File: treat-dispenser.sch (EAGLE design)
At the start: 36 parts, among them U1 MCP73831, U3 ATMEGA32U4, Y1 16MHz

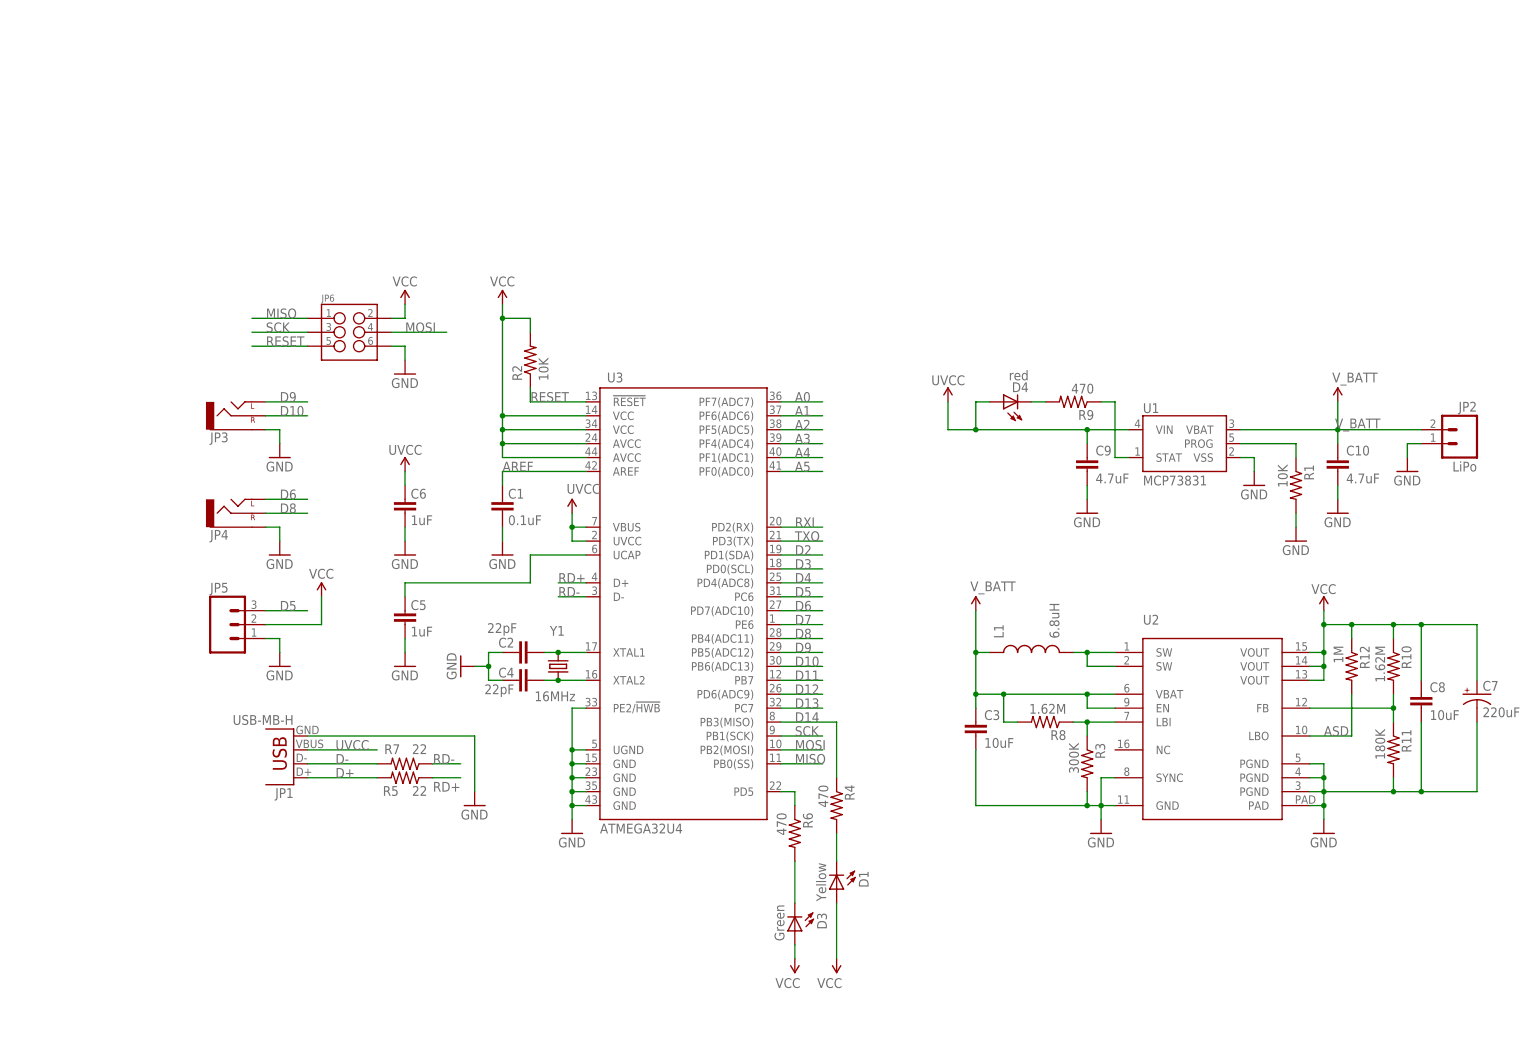
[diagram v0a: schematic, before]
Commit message: fixed some routing issues, added part numbers
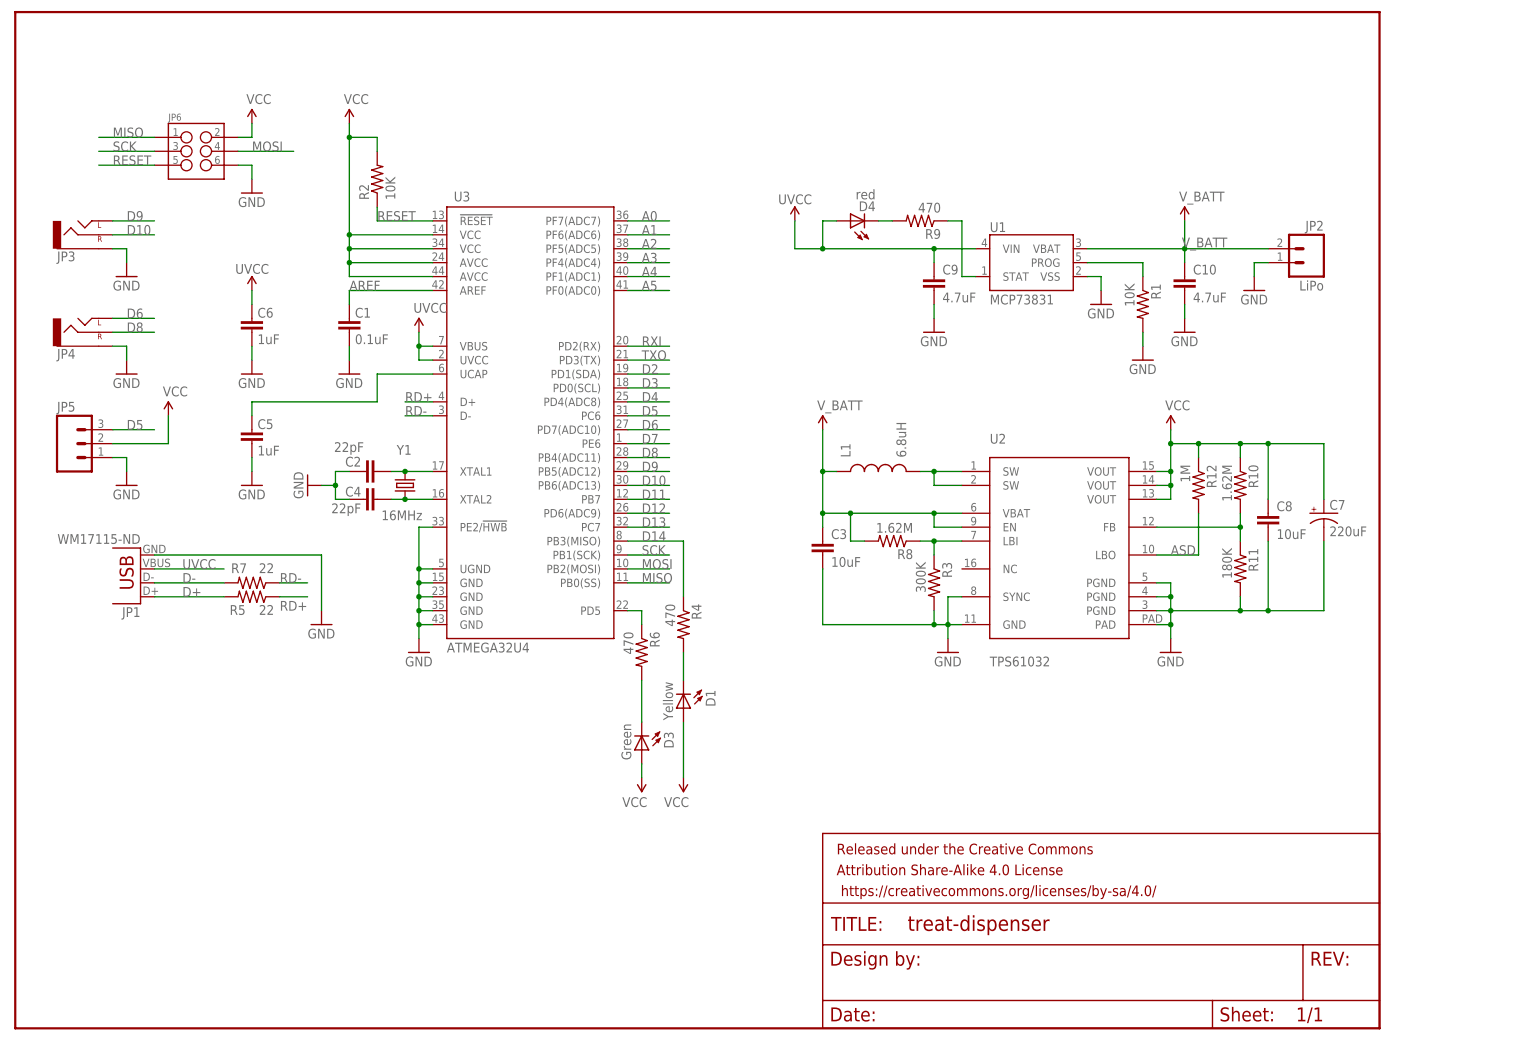
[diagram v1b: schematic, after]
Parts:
- added FRAME1: FRAME-LETTER, SparkFun-Aesthetics:FRAME-LETTER
- JP1: value USB-MB-H -> WM17115-ND
- U2: value (none) -> TPS61032
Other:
- moved on the sheet: C1, C10, C2, C3, C4, C5, C6, C7, C8, C9, D1, D3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

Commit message: minor fixes and part changes, added status led
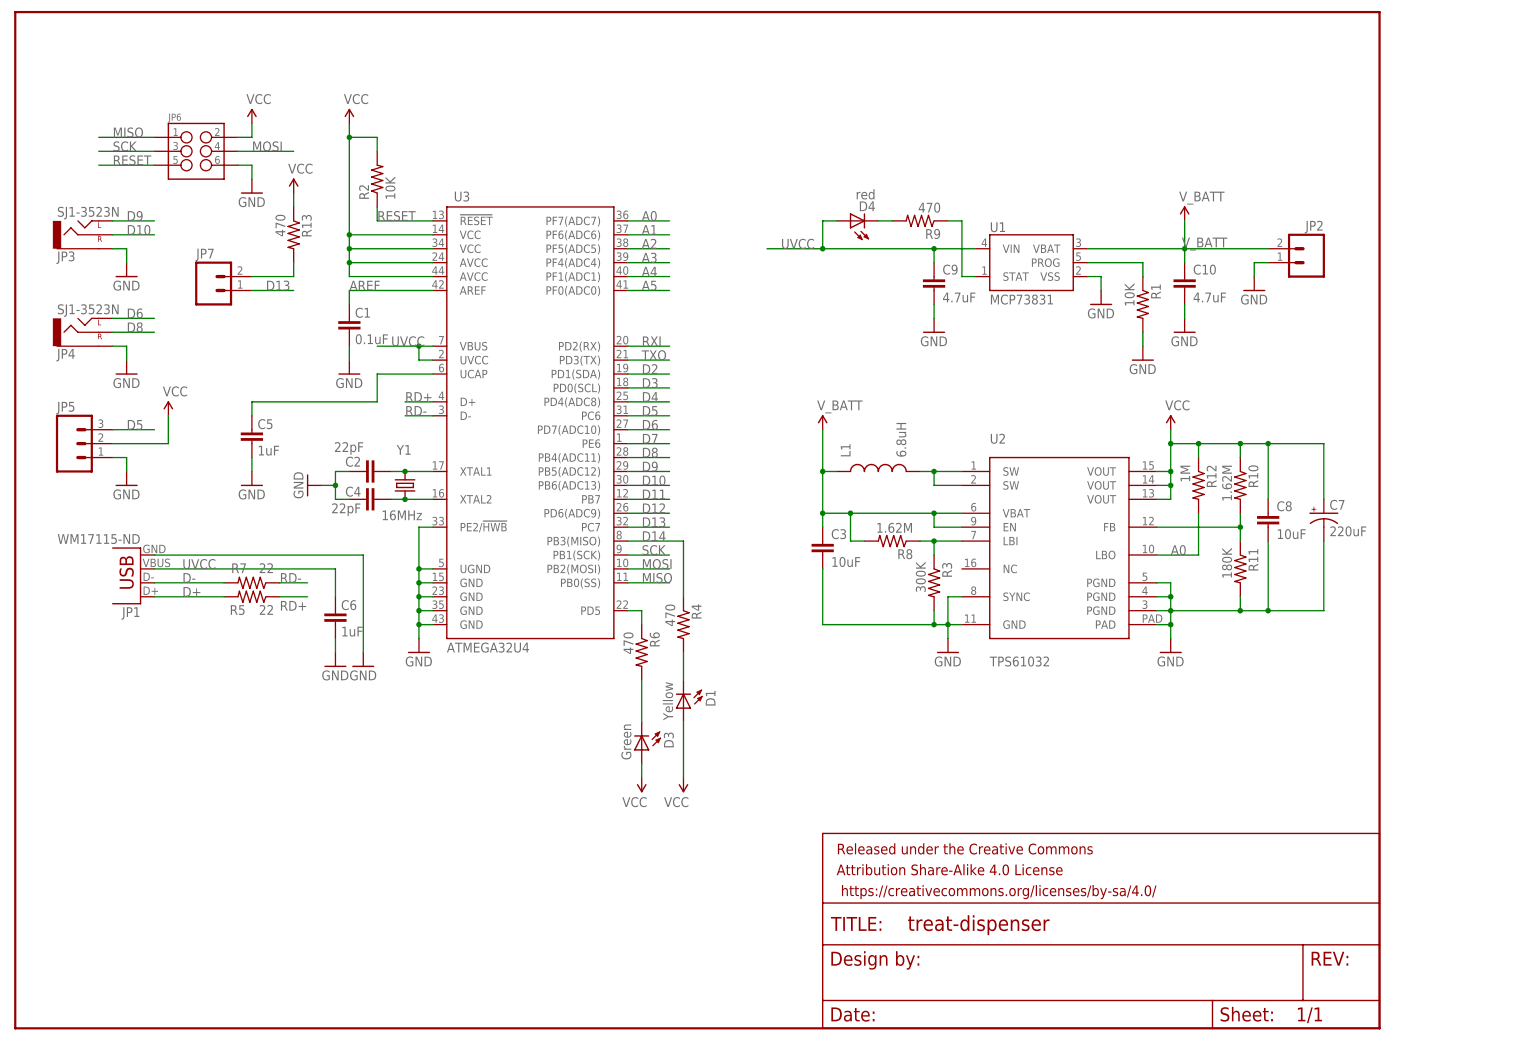
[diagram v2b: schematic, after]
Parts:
- added JP7: (no value), SparkFun-Connectors:M02PTH
- added R13: 470, SparkFun:RESISTOR0603-RES
- JP2: value LiPo -> (none); device SparkFun:M02-JST-2MM-SMT -> SparkFun-Connectors:M02JST-PTH-2-KIT
- JP3, JP4: value (none) -> SJ1-3523N
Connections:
- removed net ASD: R12.2, U2.LBO
- new net N$8: JP7.2, R13.2
- net A0: now also R12.2, U2.LBO
- net D13: now also JP7.1
- net VCC: now also R13.1
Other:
- moved on the sheet: C6
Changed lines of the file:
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@@
 <part name="C5" library="SparkFun" deviceset="CAP" device="0603-CAP" value="1uF"/>
 <part name="GND6" library="SparkFun" deviceset="GND" device=""/>
-<part name="UVCC" library="SparkFun" deviceset="3.3V" device="" value="UVCC"/>
 <part name="C6" library="SparkFun" deviceset="CAP" device="0603-CAP" value="1uF"/>
-<part name="UVCC+1" library="SparkFun" deviceset="3.3V" device="" value="UVCC"/>
 <part name="GND9" library="SparkFun" deviceset="GND" device=""/>
 <part name="R4" library="SparkFun" deviceset="RESISTOR" device="0603-RES" value="470"/>
@@
 <part name="GND14" library="supply1" deviceset="GND" device=""/>
 <part name="GND17" library="supply1" deviceset="GND" device=""/>
-<part name="JP2" library="SparkFun" deviceset="M02" device="-JST-2MM-SMT" value="LiPo"/>
 <part name="GND1" library="supply1" deviceset="GND" device=""/>
 <part name="U2" library="tps6103x" deviceset="TPS6103X" device="" value="TPS61032"/>
 <part name="GND5" library="supply1" deviceset="GND" device=""/>
 <part name="GND8" library="supply1" deviceset="GND" device=""/>
-<part name="UVCC+3" library="SparkFun" deviceset="3.3V" device="" value="UVCC"/>
 <part name="R3" library="SparkFun" deviceset="RESISTOR" device="0603-RES" value="300K"/>
 <part name="R8" library="SparkFun" deviceset="RESISTOR" device="0603-RES" value="1.62M"/>
@@
 <part name="R10" library="SparkFun" deviceset="RESISTOR" device="0603-RES" value="1.62M"/>
 <part name="R11" library="SparkFun" deviceset="RESISTOR" device="0603-RES" value="180K"/>
-<part name="JP3" library="SparkFun-Connectors" deviceset="AUDIO-JACK" device="PTH"/>
-<part name="JP4" library="SparkFun-Connectors" deviceset="AUDIO-JACK" device="PTH"/>
+<part name="JP3" library="SparkFun-Connectors" deviceset="AUDIO-JACK" device="PTH" value="SJ1-3523N"/>
+<part name="JP4" library="SparkFun-Connectors" deviceset="AUDIO-JACK" device="PTH" value="SJ1-3523N"/>
 <part name="JP5" library="SparkFun-Connectors" deviceset="M03" device="PTH"/>
 <part name="GND10" library="supply1" deviceset="GND" device=""/>
@@
 <part name="SUPPLY6" library="SparkFun-Aesthetics" deviceset="VCC" device=""/>
 <part name="FRAME1" library="SparkFun-Aesthetics" deviceset="FRAME-LETTER" device=""/>
+<part name="JP2" library="SparkFun-Connectors" deviceset="M02" device="JST-PTH-2-KIT"/>
+<part name="JP7" library="SparkFun-Connectors" deviceset="M02" device="PTH"/>
+<part name="R13" library="SparkFun" deviceset="RESISTOR" device="0603-RES" value="470"/>
+<part name="SUPPLY7" library="SparkFun-Aesthetics" deviceset="VCC" device=""/>
 </parts>
 <sheets>
@@
 </instance>
 <instance part="GND6" gate="1" x="43.18" y="99.06"/>
-<instance part="UVCC" gate="G$1" x="73.66" y="127"/>
-<instance part="C6" gate="G$1" x="43.18" y="129.54" smashed="yes" rot="R180">
-<attribute name="NAME" x="44.196" y="129.667" size="1.778" layer="95"/>
-<attribute name="VALUE" x="44.196" y="124.841" size="1.778" layer="96"/>
-</instance>
-<instance part="UVCC+1" gate="G$1" x="43.18" y="134.62" smashed="yes">
-<attribute name="VALUE" x="40.132" y="137.668" size="1.778" layer="96"/>
-</instance>
-<instance part="GND9" gate="1" x="43.18" y="119.38"/>
+<instance part="C6" gate="G$1" x="58.42" y="76.2" smashed="yes" rot="R180">
+<attribute name="NAME" x="59.436" y="76.327" size="1.778" layer="95"/>
+<attribute name="VALUE" x="59.436" y="71.501" size="1.778" layer="96"/>
+</instance>
+<instance part="GND9" gate="1" x="58.42" y="66.04"/>
 <instance part="R4" gate="G$1" x="121.92" y="73.66" rot="R270"/>
 <instance part="D1" gate="G$1" x="121.92" y="58.42" smashed="yes" rot="R180">
@@
 <attribute name="VALUE" x="44.45" y="83.058" size="1.778" layer="96"/>
 </instance>
-<instance part="GND3" gate="1" x="55.88" y="73.66"/>
+<instance part="GND3" gate="1" x="63.5" y="66.04"/>
 <instance part="P+1" gate="1" x="114.3" y="45.72" rot="R180"/>
 <instance part="P+2" gate="1" x="121.92" y="45.72" rot="R180"/>
@@
 <instance part="GND14" gate="1" x="198.12" y="132.08"/>
 <instance part="GND17" gate="1" x="205.74" y="121.92"/>
-<instance part="JP2" gate="G$1" x="236.22" y="139.7" rot="MR0"/>
 <instance part="GND1" gate="1" x="226.06" y="134.62"/>
 <instance part="U2" gate="G$1" x="190.5" y="86.36"/>
 <instance part="GND5" gate="1" x="170.18" y="68.58"/>
 <instance part="GND8" gate="1" x="210.82" y="68.58"/>
-<instance part="UVCC+3" gate="G$1" x="142.24" y="147.32" smashed="yes">
-<attribute name="VALUE" x="139.192" y="150.368" size="1.778" layer="96"/>
-</instance>
 <instance part="R3" gate="G$1" x="167.64" y="81.28" rot="R270"/>
 <instance part="R8" gate="G$1" x="160.02" y="88.9" rot="R180"/>
@@
 <instance part="FRAME1" gate="G$1" x="0" y="0"/>
 <instance part="FRAME1" gate="V" x="147.32" y="0"/>
+<instance part="JP2" gate="G$1" x="236.22" y="139.7" rot="MR0"/>
+<instance part="JP7" gate="G$1" x="35.56" y="134.62"/>
+<instance part="R13" gate="G$1" x="50.8" y="144.78" rot="R270"/>
+<instance part="SUPPLY7" gate="G$1" x="50.8" y="152.4"/>
 </instances>
 <busses>
@@
 </segment>
 <segment>
-<wire x1="43.18" y1="124.46" x2="43.18" y2="121.92" width="0.1524" layer="91"/>
+<wire x1="58.42" y1="71.12" x2="58.42" y2="68.58" width="0.1524" layer="91"/>
 <pinref part="C6" gate="G$1" pin="1"/>
 <pinref part="GND9" gate="1" pin="GND"/>
 </segment>
 <segment>
-<wire x1="55.88" y1="86.36" x2="55.88" y2="76.2" width="0.1524" layer="91"/>
+<wire x1="63.5" y1="86.36" x2="63.5" y2="68.58" width="0.1524" layer="91"/>
 <pinref part="GND3" gate="1" pin="GND"/>
-<wire x1="55.88" y1="86.36" x2="25.4" y2="86.36" width="0.1524" layer="91"/>
+<wire x1="63.5" y1="86.36" x2="25.4" y2="86.36" width="0.1524" layer="91"/>
 <pinref part="JP1" gate="G$1" pin="GND"/>
 </segment>
@@
 </segment>
 <segment>
-<pinref part="JP2" gate="G$1" pin="1"/>
 <pinref part="GND1" gate="1" pin="GND"/>
 <wire x1="228.6" y1="139.7" x2="226.06" y2="139.7" width="0.1524" layer="91"/>
 <wire x1="226.06" y1="139.7" x2="226.06" y2="137.16" width="0.1524" layer="91"/>
+<pinref part="JP2" gate="G$1" pin="1"/>
 </segment>
 <segment>
@@
 <pinref part="SUPPLY5" gate="G$1" pin="VCC"/>
 </segment>
+<segment>
+<pinref part="R13" gate="G$1" pin="1"/>
+<pinref part="SUPPLY7" gate="G$1" pin="VCC"/>
+<wire x1="50.8" y1="149.86" x2="50.8" y2="152.4" width="0.1524" layer="91"/>
+</segment>
 </net>
 <net name="D9" class="0">
@@
 <label x="114.3" y="147.32" size="1.778" layer="95"/>
 <pinref part="U3" gate="G$1" pin="PF7(ADC7)"/>
+</segment>
+<segment>
+<pinref part="R12" gate="G$1" pin="2"/>
+<wire x1="215.9" y1="93.98" x2="215.9" y2="86.36" width="0.1524" layer="91"/>
+<pinref part="U2" gate="G$1" pin="LBO"/>
+<wire x1="215.9" y1="86.36" x2="208.28" y2="86.36" width="0.1524" layer="91"/>
+<label x="210.82" y="86.36" size="1.778" layer="95"/>
 </segment>
 </net>
@@
 <label x="114.3" y="91.44" size="1.778" layer="95"/>
 <pinref part="U3" gate="G$1" pin="PC7"/>
+</segment>
+<segment>
+<pinref part="JP7" gate="G$1" pin="1"/>
+<wire x1="43.18" y1="134.62" x2="50.8" y2="134.62" width="0.1524" layer="91"/>
+<label x="45.72" y="134.62" size="1.778" layer="95"/>
 </segment>
 </net>
@@
 <pinref part="C10" gate="G$1" pin="1"/>
 <pinref part="U1" gate="G$1" pin="VBAT"/>
-<pinref part="JP2" gate="G$1" pin="2"/>
 <pinref part="SUPPLY1" gate="G$1" pin="V_BATT"/>
 <wire x1="213.36" y1="142.24" x2="213.36" y2="147.32" width="0.1524" layer="91"/>
+<pinref part="JP2" gate="G$1" pin="2"/>
 </segment>
 <segment>
@@
 <net name="UVCC" class="0">
 <segment>
-<wire x1="25.4" y1="83.82" x2="38.1" y2="83.82" width="0.1524" layer="91"/>
 <label x="30.48" y="83.82" size="1.778" layer="95"/>
 <pinref part="JP1" gate="G$1" pin="VBUS"/>
+<wire x1="58.42" y1="83.82" x2="58.42" y2="78.74" width="0.1524" layer="91"/>
+<pinref part="C6" gate="G$1" pin="2"/>
+<wire x1="25.4" y1="83.82" x2="58.42" y2="83.82" width="0.1524" layer="91"/>
 </segment>
 <segment>
@@
 <wire x1="149.86" y1="147.32" x2="147.32" y2="147.32" width="0.1524" layer="91"/>
 <wire x1="147.32" y1="147.32" x2="147.32" y2="142.24" width="0.1524" layer="91"/>
-<wire x1="142.24" y1="142.24" x2="147.32" y2="142.24" width="0.1524" layer="91"/>
+<wire x1="137.16" y1="142.24" x2="147.32" y2="142.24" width="0.1524" layer="91"/>
 <junction x="167.64" y="142.24"/>
 <junction x="147.32" y="142.24"/>
@@
 <pinref part="C9" gate="G$1" pin="1"/>
 <pinref part="D4" gate="G$1" pin="A"/>
-<pinref part="UVCC+3" gate="G$1" pin="3.3V"/>
-<wire x1="142.24" y1="142.24" x2="142.24" y2="147.32" width="0.1524" layer="91"/>
+<label x="139.7" y="142.24" size="1.778" layer="95"/>
 </segment>
 <segment>
@@
 <wire x1="76.2" y1="121.92" x2="73.66" y2="121.92" width="0.1524" layer="91"/>
 <wire x1="73.66" y1="121.92" x2="73.66" y2="124.46" width="0.1524" layer="91"/>
-<wire x1="73.66" y1="127" x2="73.66" y2="124.46" width="0.1524" layer="91"/>
+<wire x1="66.04" y1="124.46" x2="73.66" y2="124.46" width="0.1524" layer="91"/>
 <junction x="73.66" y="124.46"/>
 <pinref part="U3" gate="G$1" pin="VBUS"/>
 <pinref part="U3" gate="G$1" pin="UVCC"/>
-<pinref part="UVCC" gate="G$1" pin="3.3V"/>
-</segment>
-<segment>
-<wire x1="43.18" y1="134.62" x2="43.18" y2="132.08" width="0.1524" layer="91"/>
-<pinref part="C6" gate="G$1" pin="2"/>
-<pinref part="UVCC+1" gate="G$1" pin="3.3V"/>
-</segment>
-</net>
-<net name="ASD" class="0">
-<segment>
-<pinref part="R12" gate="G$1" pin="2"/>
-<wire x1="215.9" y1="93.98" x2="215.9" y2="86.36" width="0.1524" layer="91"/>
-<pinref part="U2" gate="G$1" pin="LBO"/>
-<wire x1="215.9" y1="86.36" x2="208.28" y2="86.36" width="0.1524" layer="91"/>
-<label x="210.82" y="86.36" size="1.778" layer="95"/>
+<label x="68.58" y="124.46" size="1.778" layer="95"/>
 </segment>
 </net>
@@
 </segment>
 </net>
+<net name="N$8" class="0">
+<segment>
+<pinref part="R13" gate="G$1" pin="2"/>
+<wire x1="50.8" y1="139.7" x2="50.8" y2="137.16" width="0.1524" layer="91"/>
+<pinref part="JP7" gate="G$1" pin="2"/>
+<wire x1="50.8" y1="137.16" x2="43.18" y2="137.16" width="0.1524" layer="91"/>
+</segment>
+</net>
